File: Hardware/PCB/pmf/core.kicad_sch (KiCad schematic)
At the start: 39 parts, among them U1 AS3320, U2 TL072

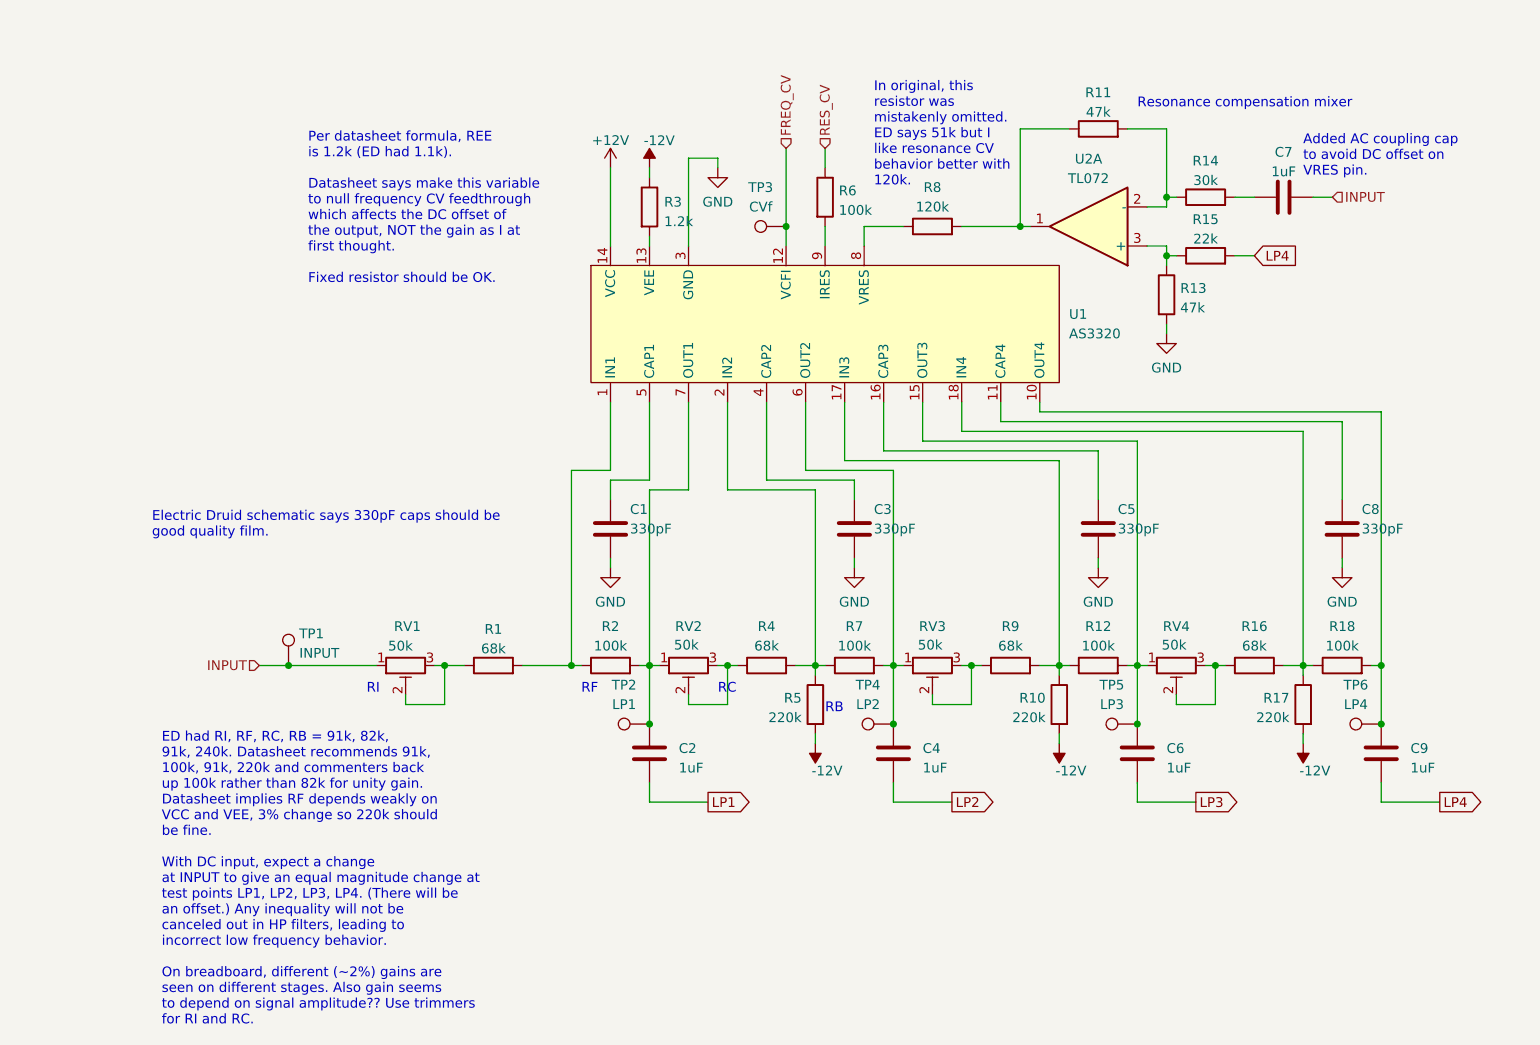
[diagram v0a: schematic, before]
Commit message: Return to smaller trimmer values; make core schematic clearer; restore munged footprints
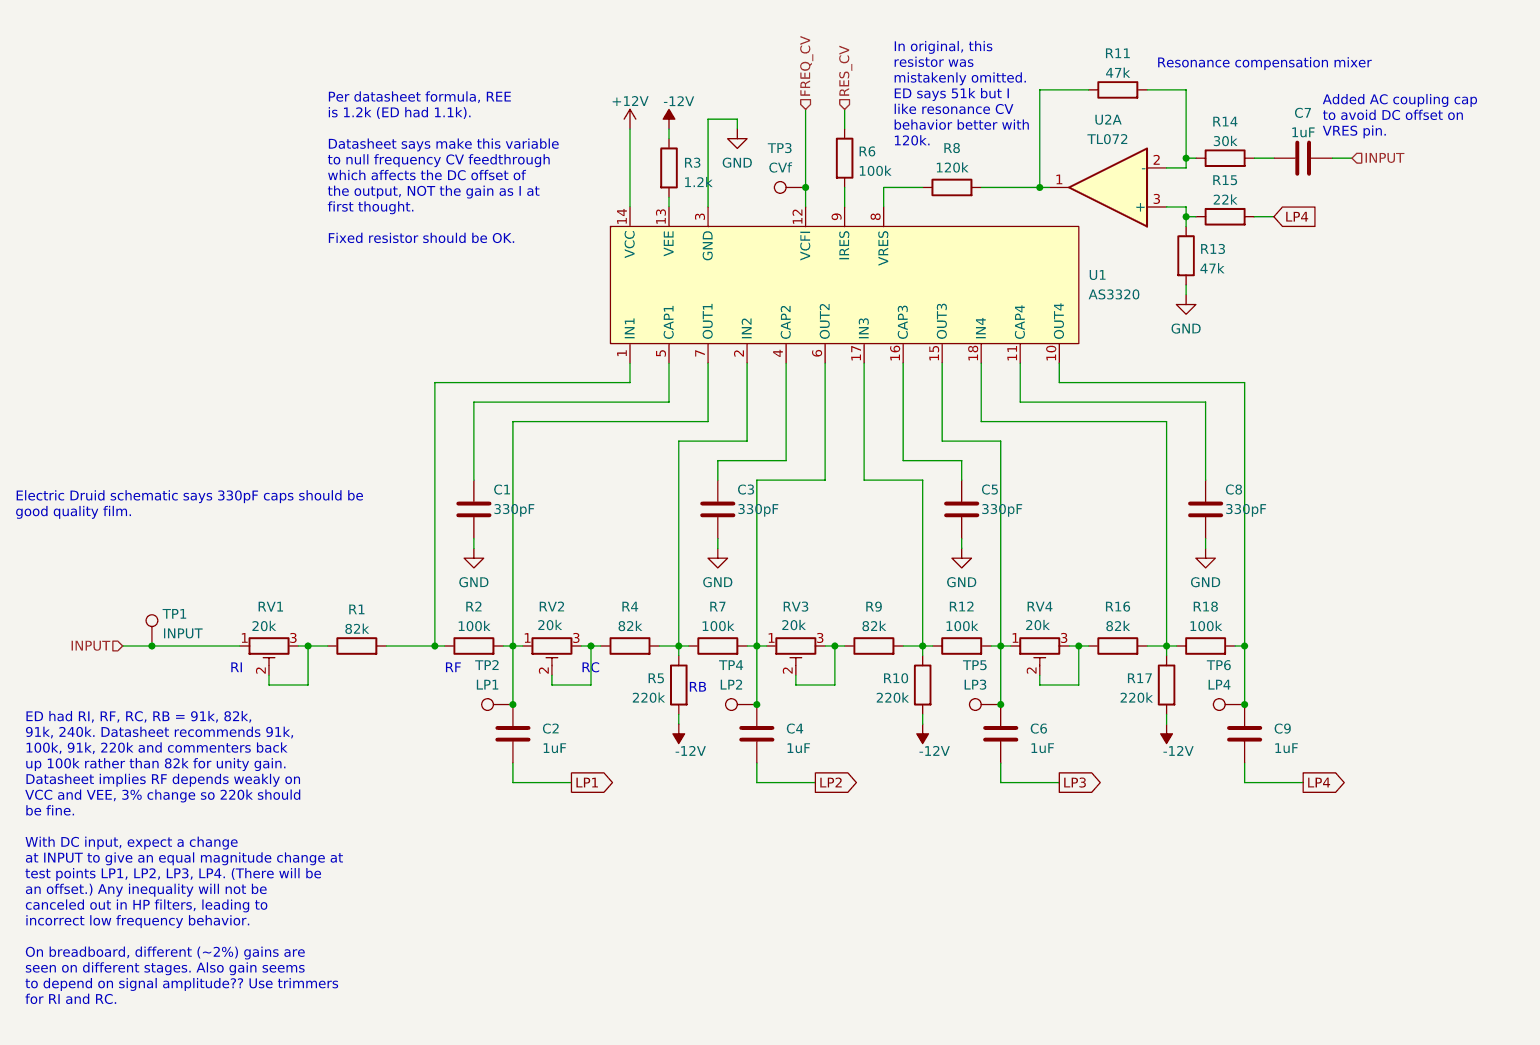
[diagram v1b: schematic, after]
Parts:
- C1, C3, C5, C8: footprint AO_tht:C_Disc_D3.0mm_W1.6mm_P2.50mm -> AO_tht:C_Rect_L7.2mm_W2.5mm_P5.00mm_FKS2_FKP2_MKS2_MKP2
- C2, C4, C6, C7, C9: footprint AO_tht:C_Disc_D3.0mm_W1.6mm_P2.50mm -> AO_tht:C_Rect_L7.2mm_W7.2mm_P5.00mm_FKS2_FKP2_MKS2_MKP2
- R1, R16, R4, R9: value 68k -> 82k
- RV1, RV2, RV3, RV4: value 50k -> 20k
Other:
- moved on the sheet: C1, C2, C3, C4, C5, C6, C7, C8, C9, R1, R10, R11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

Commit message: Pre fab tweaks, Gerbers, BOM
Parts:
- U1: Manufacturer (none) -> Alfa
- renumbered C8 to C7, C9 to C8, C7 to C9, R8 to R10, R12 to R11, R11 to R12, R16 to R13, R17 to R14, R13 to R15, R18 to R16, R14 to R17, R15 to R18, R4 to R3, R3 to R4, R7 to R6, R6 to R7, R9 to R8, R10 to R9, TP4 to TP3, TP3 to TP4

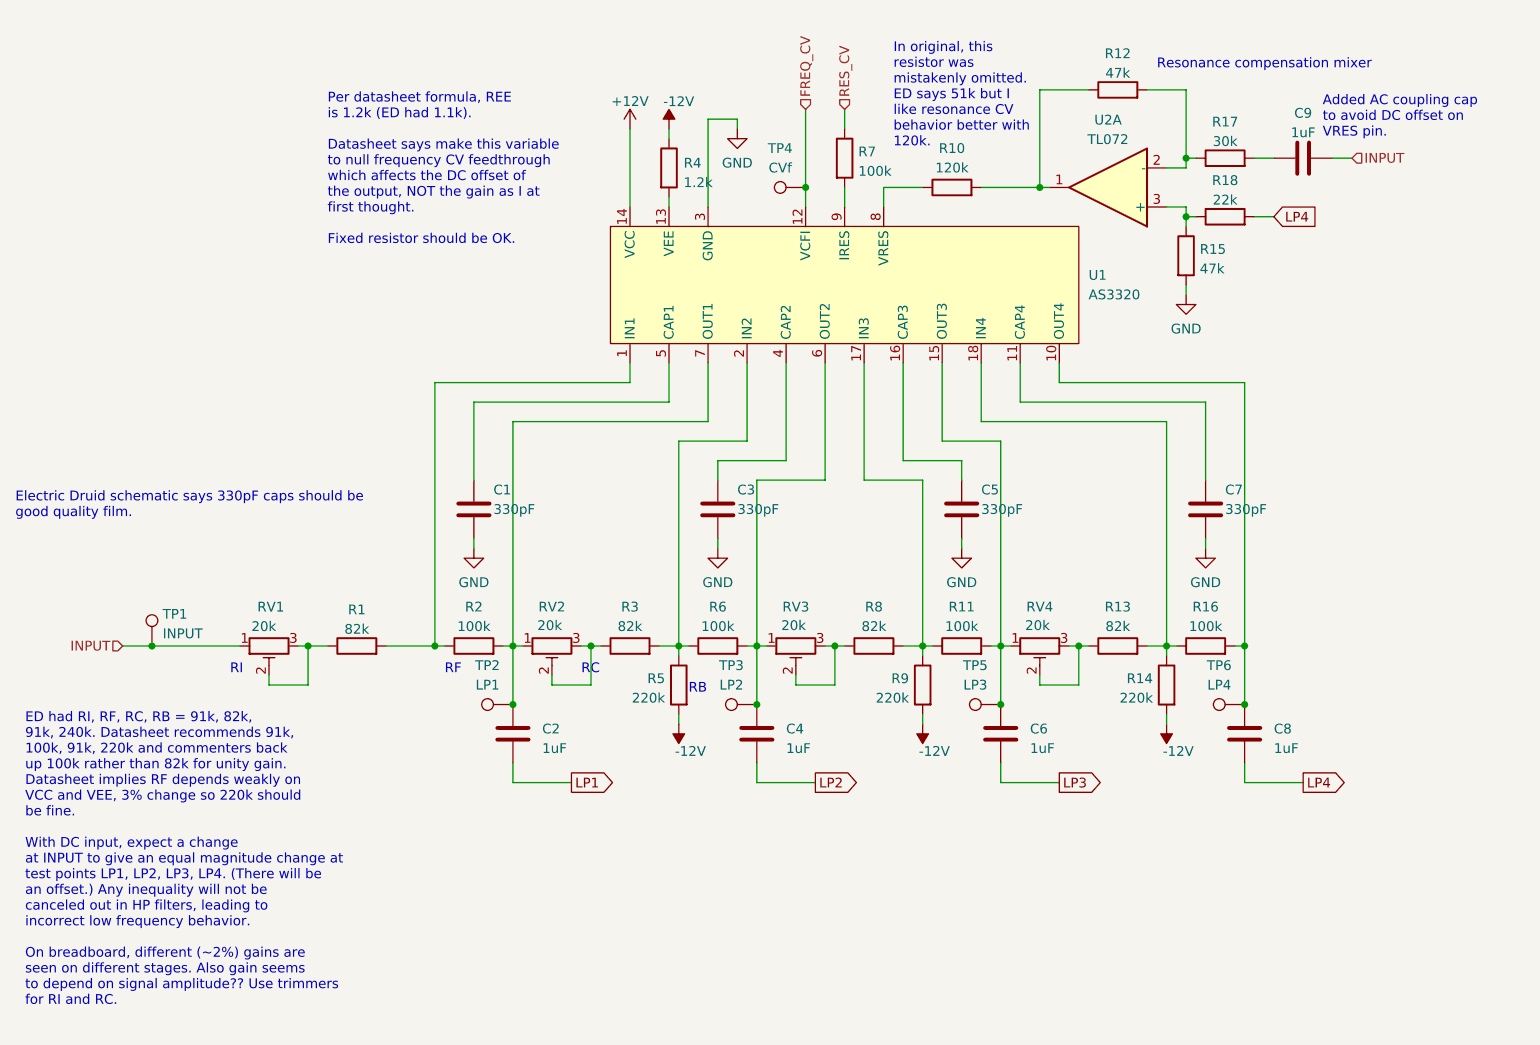
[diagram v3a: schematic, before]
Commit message: Text boxes
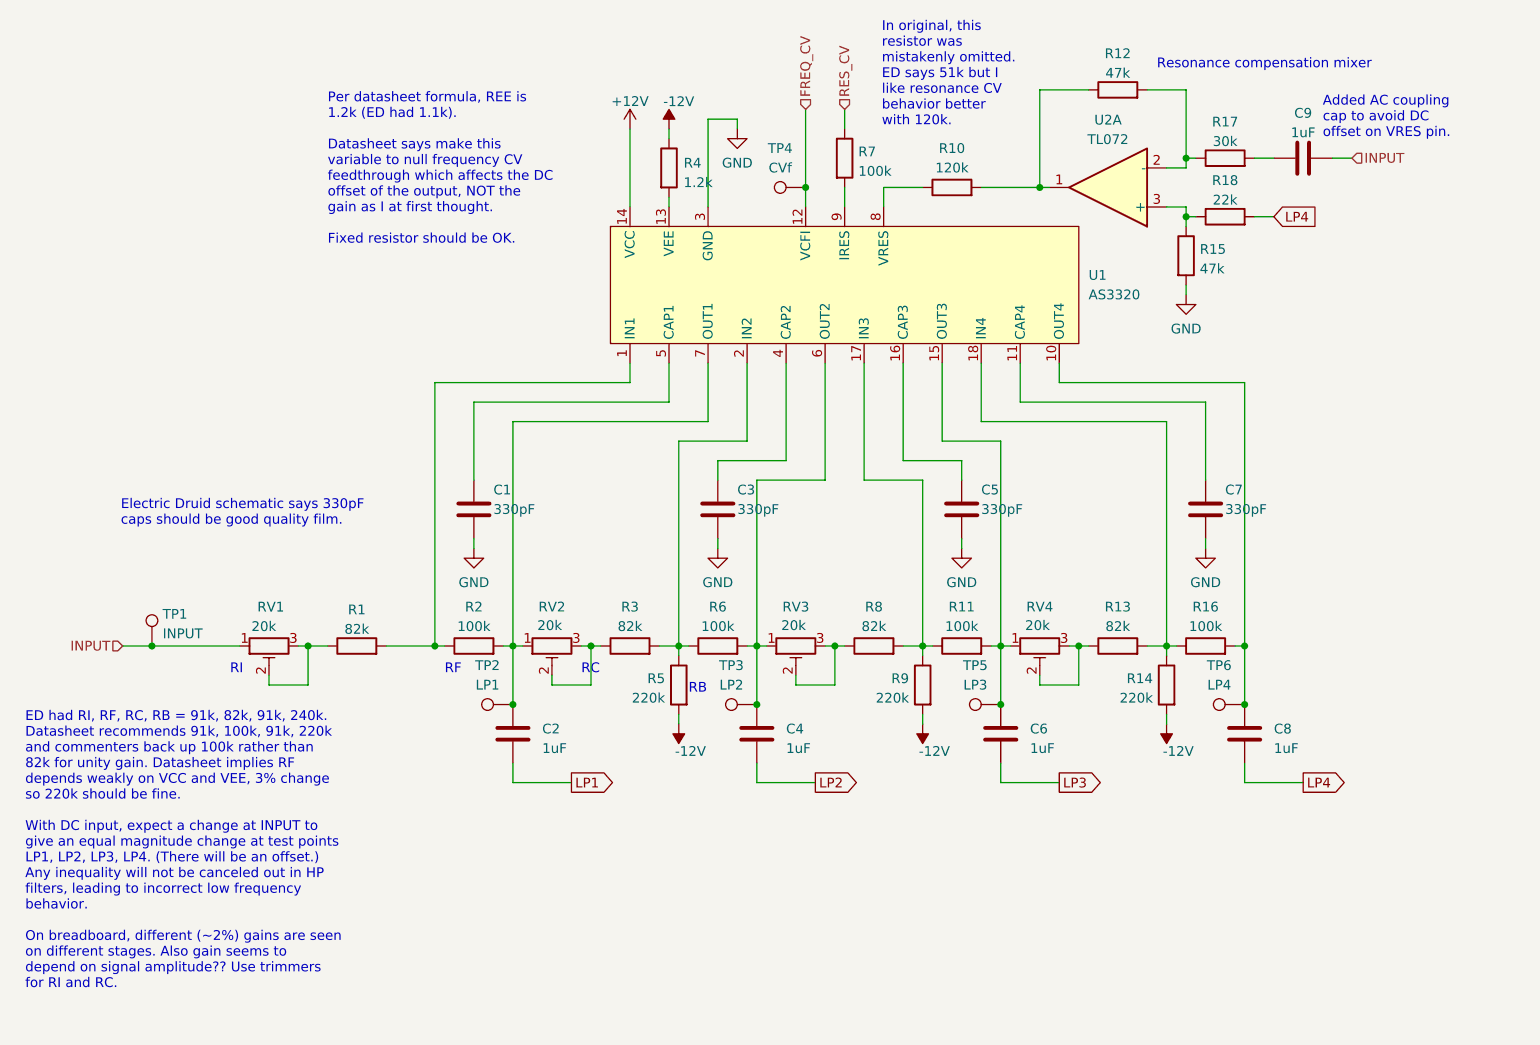
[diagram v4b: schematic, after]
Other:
- note removed: "Added AC coupling cap to avoid DC offset on VRES pin."
- note removed: "ED had RI, RF, RC, RB = 91k, 82k, 91k, 240k. Datasheet recommends 91k, 100k, 91k, 220k and commenters back up 100k rather than 82k for unity gain. Datasheet implies RF depends weakly on VCC and VEE, 3% change so 220k should be fine. With DC input, expect a change at INPUT to give an equal magnitude change at test points LP1, LP2, LP3, LP4. (There will be an offset.) Any inequality will not be can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"
- note removed: "Electric Druid schematic says 330pF caps should be good quality film."
- note removed: "In original, this resistor was mistakenly omitted. ED says 51k but I like resonance CV behavior better with 120k."
- note removed: "Per datasheet formula, REE is 1.2k (ED had 1.1k). Datasheet says make this variable to null frequency CV feedthrough which affects the DC offset of the output, NOT the gain as I at first thought. Fixed resistor should be OK."
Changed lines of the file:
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@@
     (stroke (width 0) (type default))
+  )
+  (text_box "Added AC coupling cap to avoid DC offset on VRES pin.\n"
+    (at 205.994 42.7322 0) (size 23.9848 7.8138)
+    (stroke (width -0.0001) (type default))
+    (fill (type none))
+    (effects (font (size 1.27 1.27)) (justify left top))
+  )
+  (text_box "Electric Druid schematic says 330pF caps should be good quality film."
+    (at 49.53 95.25 0) (size 39.116 5.7564)
+    (stroke (width -0.0001) (type default))
+    (fill (type none))
+    (effects (font (size 1.27 1.27)) (justify left top))
+  )
+  (text_box "In original, this resistor was mistakenly omitted. ED says 51k but I like resonance CV behavior better with 120k."
+    (at 148.59 33.02 0) (size 21.1668 16.0434)
+    (stroke (width -0.0001) (type default))
+    (fill (type none))
+    (effects (font (size 1.27 1.27)) (justify left top))
+  )
+  (text_box "ED had RI, RF, RC, RB = 91k, 82k, 91k, 240k. Datasheet recommends 91k, 100k, 91k, 220k and commenters back up 100k rather than 82k for unity gain. Datasheet implies RF depends weakly on VCC and VEE, 3% change so 220k should be fine.\n\nWith DC input, expect a change at INPUT to give an equal magnitude change at test points LP1, LP2, LP3, LP4. (There will be an offset.) Any inequality will not be canceled out in HP filters, leading to incorrect low frequency behavior.\n\nOn breadboard, different (~2%) gains are seen on different stages. Also gain seems to depend on signal amplitude?? Use trimmers for RI and RC."
+    (at 37.084 122.8438 0) (size 48.1507 40.7322)
+    (stroke (width -0.0001) (type default))
+    (fill (type none))
+    (effects (font (size 1.27 1.27)) (justify left top))
+  )
+  (text_box "Per datasheet formula, REE is 1.2k (ED had 1.1k).\n\nDatasheet says make this variable to null frequency CV feedthrough which affects the DC offset of the output, NOT the gain as I at first thought. \n\nFixed resistor should be OK."
+    (at 76.454 42.3004 0) (size 34.8463 22.2156)
+    (stroke (width -0.0001) (type default))
+    (fill (type none))
+    (effects (font (size 1.27 1.27)) (justify left top))
   )
   (text "RC" (at 110.49 119.38 0)
@@
     (effects (font (size 1.27 1.27)) (justify left bottom))
   )
-  (text "Added AC coupling cap\nto avoid DC offset on\nVRES pin.\n"
-    (at 207.01 49.53 0)
-    (effects (font (size 1.27 1.27)) (justify left bottom))
-  )
   (text "RF" (at 92.71 119.38 0)
-    (effects (font (size 1.27 1.27)) (justify left bottom))
-  )
-  (text "Per datasheet formula, REE\nis 1.2k (ED had 1.1k).\n\nDatasheet says make this variable\nto null frequency CV feedthrough\nwhich affects the DC offset of \nthe output, NOT the gain as I at\nfirst thought. \n\nFixed resistor should be OK."
-    (at 77.47 63.5 0)
     (effects (font (size 1.27 1.27)) (justify left bottom))
   )
@@
     (effects (font (size 1.27 1.27)) (justify left bottom))
   )
-  (text "In original, this\nresistor was\nmistakenly omitted.\nED says 51k but I\nlike resonance CV\nbehavior better with\n120k."
-    (at 151.13 50.8 0)
-    (effects (font (size 1.27 1.27)) (justify left bottom))
-  )
-  (text "ED had RI, RF, RC, RB = 91k, 82k, \n91k, 240k. Datasheet recommends 91k, \n100k, 91k, 220k and commenters back \nup 100k rather than 82k for unity gain.\nDatasheet implies RF depends weakly on \nVCC and VEE, 3% change so 220k should \nbe fine.\n\nWith DC input, expect a change\nat INPUT to give an equal magnitude change at \ntest points LP1, LP2, LP3, LP4. (There will be \nan offset.) Any inequality will not be \ncanceled out in HP filters, leading to\nincorrect low frequency behavior.\n\nOn breadboard, different (~2%) gains are\nseen on different stages. Also gain seems\nto depend on signal amplitude?? Use trimmers \nfor RI and RC."
-    (at 38.1 162.56 0)
-    (effects (font (size 1.27 1.27)) (justify left bottom))
-  )
   (text "RB" (at 124.46 121.92 0)
     (effects (font (size 1.27 1.27)) (justify left bottom))
   )
-  (text "Electric Druid schematic says 330pF caps should be\ngood quality film."
-    (at 36.83 99.06 0)
-    (effects (font (size 1.27 1.27)) (justify left bottom))
-  )
